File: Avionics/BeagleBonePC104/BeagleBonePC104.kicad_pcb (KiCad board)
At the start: 2 copper layers, 90.2 x 95.9 mm, 17 parts, among them U4 TJA1051T-3, U5 TMP36xS

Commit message: Ian Golberg - Tentatively Finalized v3 of the flight computer board.
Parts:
- added C2: 0.1µF, Capacitor_SMD:C_0805_2012Metric, F.Cu at (98.8, 155.4)
- added D4: CAN_PWR, LED_SMD:LED_0805_2012Metric, F.Cu at (160.9, 150.9)
- added D5: TEMP_PWR, LED_SMD:LED_0805_2012Metric, F.Cu at (160.9, 153.1)
- added D6: CLK_PWR, LED_SMD:LED_0805_2012Metric, F.Cu at (160.9, 155.3)
- added R6: 15, Resistor_SMD:R_0805_2012Metric, F.Cu at (166.0, 150.9)
- added R7: 15, Resistor_SMD:R_0805_2012Metric, F.Cu at (166.0, 153.1)
- added R8: 15, Resistor_SMD:R_0805_2012Metric, F.Cu at (166.0, 155.3)
- added TP1: TestPoint, TestPoint:TestPoint_Keystone_5000-5004_Miniature, F.Cu at (114.1, 157.2)
- added TP2: TestPoint, FlightCompuer:TestPointPad, F.Cu at (90.9, 165.8)
- added TP3: TestPoint, FlightCompuer:TestPointPad, F.Cu at (83.9, 158.6)
- added TP4: TestPoint, FlightCompuer:TestPointPad, F.Cu at (95.5, 153.9)
- added U3: ~, FlightCompuer:831054046, F.Cu at (96.2, 155.3)
- added U6: ~, FlightCompuer:SPDT Through Hole Switch, F.Cu at (143.6, 154.2)
- added U7: ~, FlightCompuer:SPDT Through Hole Switch, F.Cu at (128.3, 154.1)
- added U8: ~, FlightCompuer:SPDT Through Hole Switch, F.Cu at (133.4, 154.1)
- added U9: ~, FlightCompuer:SPDT Through Hole Switch, F.Cu at (138.4, 154.5)
- R4: value 150 -> 100; footprint Resistor_SMD:R_0603_1608Metric -> Resistor_SMD:R_0805_2012Metric
- U2: footprint PCI104Connector:PCI104ConnectorComplete -> PCI104Connector:PC104ConnectorFootprint
- moved R2 57.2 mm to (92.6, 149.4)
- moved R1 42.8 mm to (92.6, 145.1)
- moved C1 30.3 mm to (109.9, 152.6)
- moved U5 28.7 mm to (110.2, 147.1)
- moved R9 12.1 mm to (118.4, 153.3), turned to 180 degrees
- moved D3 9.02 mm to (160.9, 148.7), turned to 180 degrees
- moved U4 8.84 mm to (118.6, 147.1)
- moved R5 8.57 mm to (166.0, 148.7), turned to 0 degrees
- moved D2 7.46 mm to (160.9, 146.5), turned to 180 degrees
- moved R4 6.96 mm to (166.0, 146.5), turned to 0 degrees
- moved D1 5.59 mm to (160.9, 144.4), turned to 180 degrees
- moved R3 5.20 mm to (166.0, 144.4), turned to 0 degrees
- moved U1 0.71 mm to (170.3, 88.1)
- moved G*** 0.49 mm to (154.5, 162.6)
- moved U2 0.16 mm to (80.0, 170.0)
- renumbered R6 to R9
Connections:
- C1 pad 1: /3V3 -> Net-(D5-A)
- R1 pad 1: /5V -> Net-(R1-Pad1)
- R2 pad 1: /5V -> Net-(R1-Pad1)
- U1 pad 23: /GPIO1_17 -> /FC_TEMP
- U1 pad 5: /5V -> Net-(R1-Pad1)
- U1 pad 6: /5V -> Net-(R1-Pad1)
- U1 pad 83: unconnected-(U1-UART5_TXD-Pad83) -> /UART_TX
- U1 pad 84: unconnected-(U1-UART5_RXD-Pad84) -> /UART_RX
- U2 pad 103: unconnected-(U2-Pad103) -> /10MHz_CLK
- U2 pad 19: unconnected-(U2-UART_1_TX-Pad19) -> /UART_TX
- U2 pad 20: unconnected-(U2-UART_1_RX-Pad20) -> /UART_RX
- U2 pad 36: /GPIO2_6 -> unconnected-(U2-Pad36)
- U2 pad 53: /FC_TEMP -> unconnected-(U2-TEMP_1-Pad53)
- U2 pad 70: unconnected-(U2-Pad70) -> /GPIO2_6
- U2 pad 80: unconnected-(U2-Pad80) -> /3V3
- U2 pad 96: /GPIO1_17 -> /FC_TEMP
- U4 pad 3: /3V3 -> Net-(D4-A)
- U4 pad 5: /3V3 -> Net-(D4-A)
- U5 pad 5: /3V3 -> Net-(D5-A)
- U5 pad 8: /3V3 -> Net-(D5-A)
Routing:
- net /GPIO1_15: track 0.00 -> 0.82 mm
- added copper zone on In2.Cu, net /3V3
- added copper zone on B.Cu, net GND
- added copper zone on In1.Cu, net GND
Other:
- board size 90.2 x 95.9 mm -> 90.2 x 96 mm
- copper layers 2 -> 4
- board text added: "10MHz Clock"
- board text added: "A"
- board text added: "Beaglebone PWR"
- board text added: "CAN"
- board text added: "CAN PWR"
- board text added: "CFPPS-73"
- board text added: "CLK"
- board text added: "CLK_PWR"
- board text added: "DO NOT APPLY VOLTAGE TO ANY PC104/GPIO PIN WHEN 5V POWER IS NOT SUPPLIED TO THE BEAGLEBONE, IT WILL DAMAGE THE PROCESSOR AND VOID THE WARRANTY. NO PINS ARE TO BE DRIVEN UNTIL AFTER THE SYS_RESET LINE GOES HIGH."
- board text added: "I2C_SCL"
- board text added: "I2C_SDA"
- board text added: "PC104 3V3"
- board text added: "PC104 5V"
- board text added: "Rev. 3.0.0 - 09.5.24 - Ian Goldberg"
- board text added: "SYS_RESETn"
- board text added: "TEMP"
- board text added: "TEMP PWR"
- board text added: "TJA1051T-3"
- board text added: "TMP36xS"
- board text added: "TURN ALL SWITCHES *OFF* BEFORE POWERING BEAGLEBONE."
- board text added: "V"
- board text added: "{dblquote}Do, or do not. There is no try.{dblquote} -Yoda"
- board text removed: "Rev. 3 - 09.5.24 - Ian Goldberg"

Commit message: Ian Goldberg - Finished Rev. 3 of the Flight Computer PCB.
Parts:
- added GND: TestPoint, TestPoint:TestPoint_Keystone_5000-5004_Miniature, F.Cu at (104.9, 157.2)
- moved U7 2.22 mm to (126.1, 154.4)
- moved U8 1.94 mm to (131.5, 154.4)
- moved U9 1.60 mm to (136.8, 154.4)
- moved U6 1.43 mm to (142.1, 154.4)
- moved R9 0.73 mm to (118.6, 152.6)
- moved C1 0.30 mm to (110.2, 152.6)
- moved C2 0.10 mm to (98.8, 155.3)
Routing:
- net /5V: track 0.00 -> 148.6 mm, vias 0 -> 3
- net /10MHz_CLK: track 0.00 -> 139.2 mm, vias 0 -> 2
- net /I2C_SCL: track 0.00 -> 122.1 mm, vias 0 -> 3
- net /I2C_SDA: track 0.00 -> 121.7 mm, vias 0 -> 3
- net /SYS_RESETn: track 0.00 -> 121.5 mm, vias 0 -> 2
- net /UART_RX: track 0.00 -> 108.1 mm, vias 0 -> 3
- net /FC_TEMP: track 0.00 -> 102.9 mm, vias 0 -> 2
- net /CAN_H: track 0.00 -> 102.6 mm, vias 0 -> 2
- net /UART_TX: track 0.00 -> 102.4 mm, vias 0 -> 3
- net /CAN_L: track 0.00 -> 99.6 mm, vias 0 -> 2
- net /CAN_SLNT: track 0.00 -> 94.9 mm, vias 0 -> 3
- net Net-(D6-A): track 0.00 -> 90.4 mm, vias 0 -> 2
- net /GPIO3_20: track 0.00 -> 77.6 mm, vias 0 -> 2
- net /GPIO0_7: track 0.00 -> 71.5 mm, vias 0 -> 2
- net /GPIO1_16: track 0.00 -> 69.7 mm, vias 0 -> 2
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- added copper zone on F.Cu, net GND
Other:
- board text added: "Rev. 3.0.0 - 09.15.24 - Ian Goldberg"
- board text removed: "Rev. 3.0.0 - 09.5.24 - Ian Goldberg"

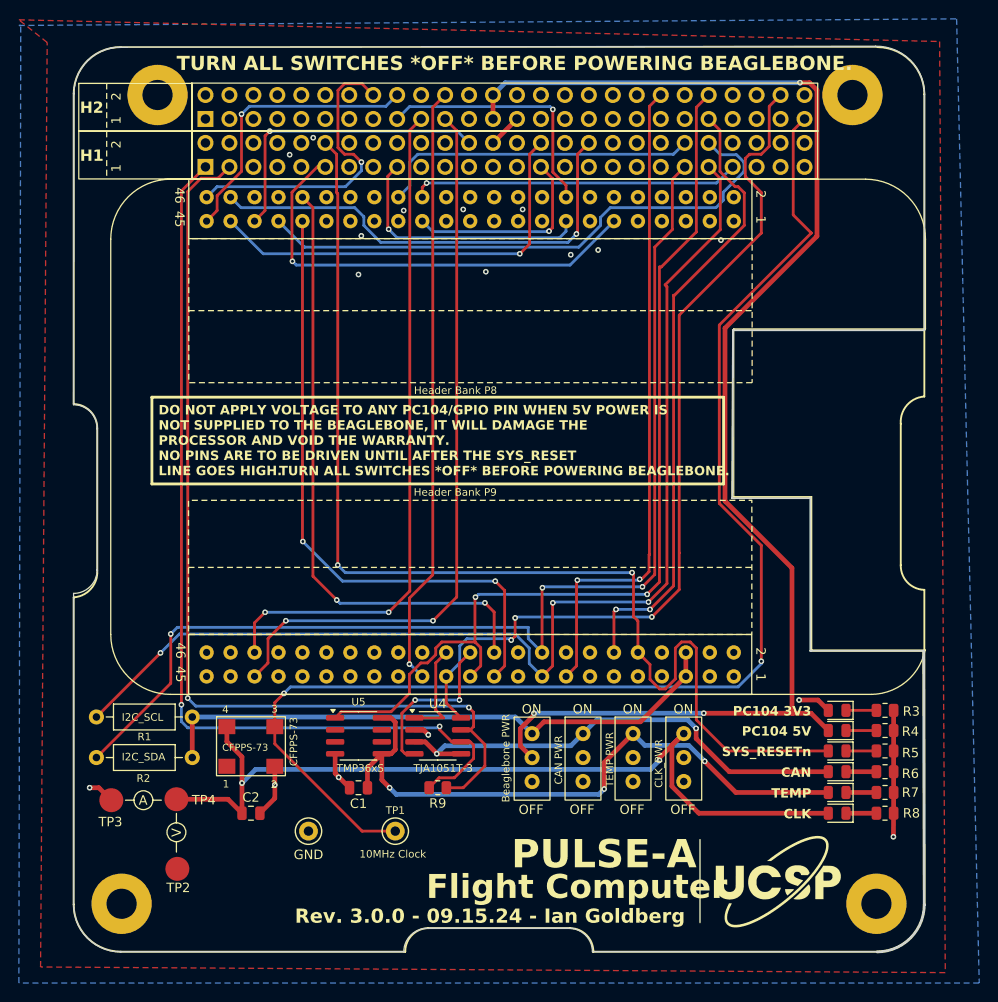
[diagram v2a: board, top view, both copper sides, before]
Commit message: Ian Goldberg - Final design for Version 3 of the Flight Computer PCB. Sending to the manufacturer now.
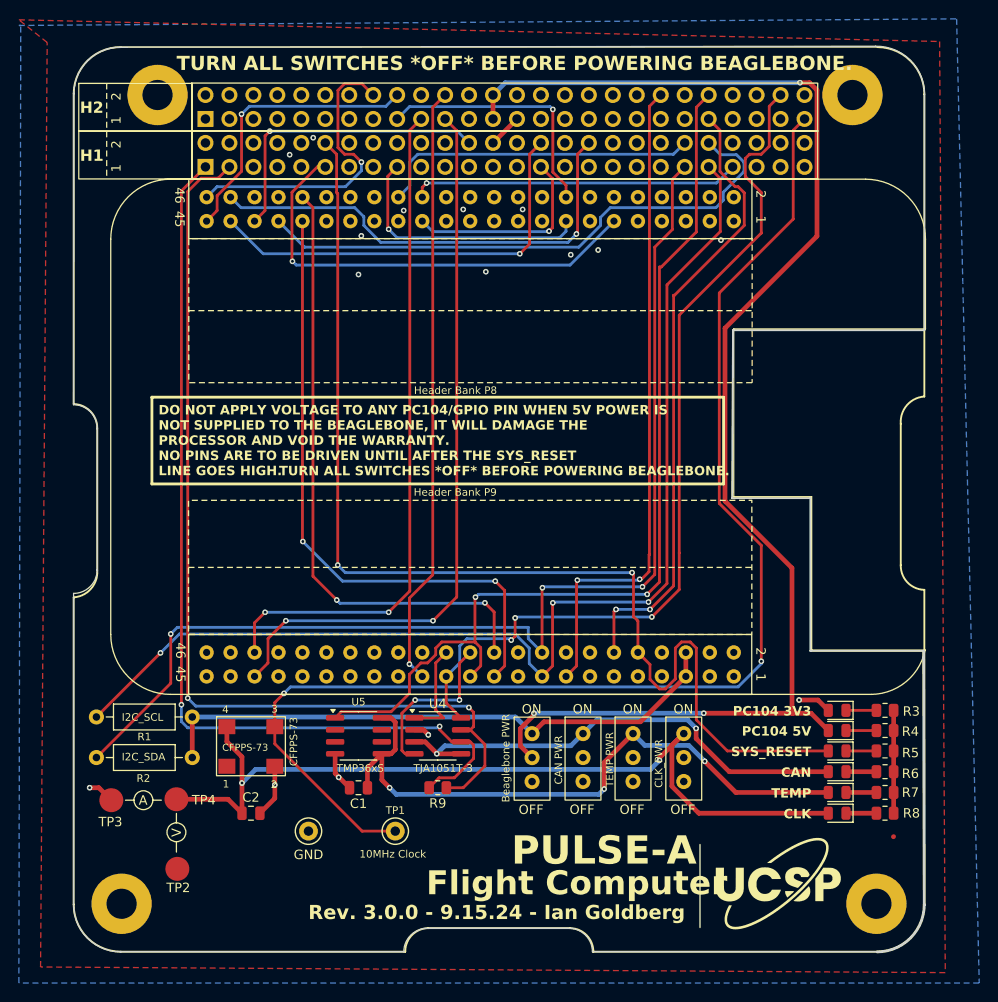
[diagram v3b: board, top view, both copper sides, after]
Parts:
- moved G*** 0.21 mm to (154.5, 162.8)
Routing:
- net GND: track 25.2 -> 22.7 mm, vias 4 -> 3
- net /10MHz_CLK: track 139.2 -> 137.6 mm
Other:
- board text added: "Rev. 3.0.0 - 9.15.24 - Ian Goldberg"
- board text added: "SYS_RESET"
- board text removed: "Rev. 3.0.0 - 09.15.24 - Ian Goldberg"
- board text removed: "SYS_RESETn"

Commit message: Ian Goldberg - Pushing preliminary versions of version 4
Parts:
- removed C2: 0.1µF, Capacitor_SMD:C_0805_2012Metric
- removed D6: CLK_PWR, LED_SMD:LED_0805_2012Metric
- removed GND, TP1: TestPoint, TestPoint:TestPoint_Keystone_5000-5004_Miniature
- removed R8: 15, Resistor_SMD:R_0805_2012Metric
- removed TP2, TP3, TP4: TestPoint, FlightCompuer:TestPointPad
- removed U6, U8, U9: ~, FlightCompuer:SPDT Through Hole Switch
- added BT1: Battery_Cell, Battery:BatteryHolder_Keystone_106_1x20mm, B.Cu at (147.0, 115.5)
- added Q1: 2N7002, Package_TO_SOT_SMD:SOT-23, F.Cu at (91.7, 146.8)
- added R12: 10k, Resistor_SMD:R_0805_2012Metric, F.Cu at (115.2, 159.2)
- added R13: 10k, Resistor_SMD:R_0805_2012Metric, F.Cu at (144.1, 154.7)
- added RTC_MFP1: TestPoint, TestPoint:TestPoint_Keystone_5000-5004_Miniature, F.Cu at (110.0, 158.9)
- added TP5: TestPoint, TestPoint:TestPoint_Keystone_5000-5004_Miniature, F.Cu at (87.9, 158.0)
- added TP6-32.768_kHz1: TestPoint, TestPoint:TestPoint_Keystone_5000-5004_Miniature, F.Cu at (87.9, 152.3)
- added U10: MCP7940N-xSN, Package_SO:SOIC-8_3.9x4.9mm_P1.27mm, F.Cu at (115.3, 147.8)
- added U12: ~, FlightCompuer:XTAL4_SiT1533_SIT, F.Cu at (115.5, 153.6)
- added U13: ~, FlightCompuer:QFN50P400X400X100-25N, F.Cu at (144.3, 147.9)
- added U14: ~, FlightCompuer:XTAL4_SiT1533_SIT, F.Cu at (135.6, 154.0)
- R1, R2: value 5.6k -> 2.2k; footprint Resistor_THT:R_Axial_DIN0207_L6.3mm_D2.5mm_P10.16mm_Horizontal -> Resistor_SMD:R_0805_2012Metric
- U3: value ~ -> W25N01GVZEIG_TR; footprint FlightCompuer:831054046 -> FlightCompuer:SON127P800X600X80-9N
- U7: value ~ -> MAX14662; footprint FlightCompuer:SPDT Through Hole Switch -> Package_DFN_QFN:QFN-28-1EP_4x4mm_P0.4mm_EP2.6x2.6mm
- moved R2 80.7 mm to (157.3, 101.2), turned to 0 degrees
- moved R1 79.9 mm to (157.3, 98.2), turned to 0 degrees
- moved U3 29.7 mm to (125.1, 148.3)
- moved R9 19.9 mm to (98.7, 153.1)
- moved U4 19.9 mm to (98.7, 147.6)
- moved U7 11.2 mm to (135.4, 148.2)
- moved C1 3.69 mm to (106.7, 153.6)
- moved U5 3.26 mm to (107.0, 147.7)
- moved G*** 1.08 mm to (154.9, 163.8)
- moved U1 0.14 mm to (170.2, 88.2)
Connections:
- C1 pad 1: Net-(D5-A) -> /TEMP_PWR
- D3 pad 2: /SYS_RESETn -> /~{SYS_RESETn}
- D4 pad 2: Net-(D4-A) -> /CAN_PWR
- D5 pad 2: Net-(D5-A) -> /TEMP_PWR
- R2 pad 1: Net-(R1-Pad1) -> /I2C_SDA
- R2 pad 2: /I2C_SDA -> Net-(R1-Pad1)
- U1 pad 11: unconnected-(U1-UART4_RXD-Pad11) -> /GPIO1_13
- U1 pad 12: /GPIO1_28 -> /GPIO1_12
- U1 pad 14: unconnected-(U1-EHRPWM1A-Pad14) -> /GPIO1_26
- U1 pad 15: /GPIO1_16 -> /GPIO1_15
- U1 pad 16: unconnected-(U1-EHRPWM1B-Pad16) -> /GPIO1_14
- U1 pad 17: /I2C_SCL -> /GPIO1_27
- U1 pad 18: /I2C_SDA -> /GPIO2_1
- U1 pad 23: /FC_TEMP -> unconnected-(U1-GPIO1_4-Pad23)
- U1 pad 27: /GPIO3_19 -> /GPI02_22
- U1 pad 28: unconnected-(U1-SPI1_CS0-Pad28) -> /GPIO2_24
- U1 pad 29: unconnected-(U1-SPI1_D0-Pad29) -> /NAND_~{WP}(I/O2)
- U1 pad 30: unconnected-(U1-SPI1_D1-Pad30) -> /NAND_~{HOLD}(I/O3)
- U1 pad 31: unconnected-(U1-SPI1_SCLK-Pad31) -> /SPI_SCLK
- U1 pad 39: unconnected-(U1-AIN0-Pad39) -> /GPIO2_12
- U1 pad 4: unconnected-(U1-DC_3.3V-Pad4) -> Net-(R1-Pad1)
- U1 pad 40: unconnected-(U1-AIN1-Pad40) -> /FC_TEMP
- U1 pad 41: /GPIO3_20 -> /GPIO2_10
- U1 pad 43: GND -> /GPIO2_8
- U1 pad 44: GND -> /GPIO2_9
- U1 pad 45: GND -> /MSP430_RST
- U1 pad 46: GND -> /10MHz_CLK_STANDBY
- U1 pad 47: GND -> (no net)
- U1 pad 48: GND -> (no net)
- U1 pad 49: unconnected-(U1-GPIO1_6-Pad49) -> (no net)
- U1 pad 5: Net-(R1-Pad1) -> /5V
- U1 pad 50: unconnected-(U1-GPIO1_7-Pad50) -> (no net)
- U1 pad 51: unconnected-(U1-GPIO1_2-Pad51) -> (no net)
- U1 pad 52: unconnected-(U1-GPIO1_3-Pad52) -> (no net)
- U1 pad 53: unconnected-(U1-TIMER4-Pad53) -> (no net)
- U1 pad 54: unconnected-(U1-TIMER7-Pad54) -> (no net)
- U1 pad 55: unconnected-(U1-TIMER5-Pad55) -> (no net)
- U1 pad 56: unconnected-(U1-TIMER6-Pad56) -> (no net)
- U1 pad 57: /GPIO1_13 -> (no net)
- U1 pad 58: /GPIO1_12 -> (no net)
- U1 pad 59: unconnected-(U1-EHRPWM2B-Pad59) -> (no net)
- U1 pad 6: Net-(R1-Pad1) -> /5V
- U1 pad 60: /GPIO1_26 -> (no net)
- U1 pad 61: /GPIO1_15 -> (no net)
- U1 pad 62: /GPIO1_14 -> (no net)
- U1 pad 63: /GPIO1_27 -> (no net)
- U1 pad 64: /GPIO2_1 -> (no net)
- U1 pad 65: unconnected-(U1-EHRPWM2A-Pad65) -> (no net)
- U1 pad 66: unconnected-(U1-GPIO1_31-Pad66) -> (no net)
- U1 pad 67: unconnected-(U1-GPIO1_30-Pad67) -> (no net)
- U1 pad 68: unconnected-(U1-GPIO1_5-Pad68) -> (no net)
- U1 pad 69: unconnected-(U1-GPIO1_4-Pad69) -> (no net)
- U1 pad 70: unconnected-(U1-GPIO1_1-Pad70) -> (no net)
- U1 pad 71: unconnected-(U1-GPIO1_0-Pad71) -> (no net)
- U1 pad 72: /GPIO1_29 -> (no net)
- U1 pad 73: /GPI02_22 -> (no net)
- U1 pad 74: /GPIO2_24 -> (no net)
- U1 pad 75: /GPIO2_23 -> (no net)
- U1 pad 76: /GPIO2_25 -> (no net)
- U1 pad 77: unconnected-(U1-UART5_CTSN-Pad77) -> (no net)
- U1 pad 78: unconnected-(U1-UART5_RTSN-Pad78) -> (no net)
- U1 pad 79: unconnected-(U1-UART4_RTSN-Pad79) -> (no net)
- U1 pad 80: unconnected-(U1-UART3_RTSN-Pad80) -> (no net)
- U1 pad 81: unconnected-(U1-UART4_CTSN-Pad81) -> (no net)
- U1 pad 82: unconnected-(U1-UART3_CTSN-Pad82) -> (no net)
- U1 pad 83: /UART_TX -> (no net)
- U1 pad 84: /UART_RX -> (no net)
- U1 pad 85: /GPIO2_12 -> (no net)
- U1 pad 86: /GPIO2_13 -> (no net)
- U1 pad 87: /GPIO2_10 -> (no net)
- U1 pad 88: /GPIO2_11 -> (no net)
- U1 pad 89: /GPIO2_8 -> (no net)
- U1 pad 90: /GPIO2_9 -> (no net)
- U1 pad 91: /GPIO2_6 -> (no net)
- U1 pad 92: /GPIO2_7 -> (no net)
- U2 pad 103: /10MHz_CLK -> unconnected-(U2-Pad103)
- U2 pad 42: /GPIO2_25 -> unconnected-(U2-Pad42)
- U2 pad 44: /GPIO2_12 -> unconnected-(U2-Pad44)
- U2 pad 46: /GPIO2_23 -> /GPIO2_12
- U2 pad 51: unconnected-(U2-Pad51) -> /SPWTDIO
- U2 pad 52: unconnected-(U2-Pad52) -> /SPWTCK
- U2 pad 68: /GPIO2_7 -> unconnected-(U2-ADCS_ENABLE-Pad68)
- U2 pad 70: /GPIO2_6 -> unconnected-(U2-ADCS_BOOT-Pad70)
- U2 pad 71: /GPIO0_7 -> unconnected-(U2-Pad71)
- U2 pad 73: /GPIO3_20 -> unconnected-(U2-Pad73)
- U2 pad 74: /GPIO3_19 -> unconnected-(U2-Pad74)
- U2 pad 92: /GPIO1_16 -> unconnected-(U2-Pad92)
- U2 pad 95: /GPIO1_28 -> unconnected-(U2-Pad95)
- U2 pad 96: /FC_TEMP -> unconnected-(U2-Pad96)
- U3 pad 1: /10MHz_CLK_STANDBY -> /SPI_CS
- U3 pad 2: GND -> /SPI_MISO
- U3 pad 3: /10MHz_CLK -> /NAND_~{WP}(I/O2)
- U3 pad 4: Net-(D6-A) -> GND
- U4 pad 3: Net-(D4-A) -> /CAN_PWR
- U4 pad 5: Net-(D4-A) -> /CAN_PWR
- U5 pad 5: Net-(D5-A) -> /TEMP_PWR
- U5 pad 8: Net-(D5-A) -> /TEMP_PWR
- U7 pad 1: Net-(R1-Pad1) -> /SWITCH_MODE_SEL
- U7 pad 2: /5V -> /3V3
- U7 pad 3: unconnected-(U7-Pad3) -> /3V3
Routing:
- net /5V: track 148.6 -> 0.00 mm, vias 3 -> 0
- net /10MHz_CLK: track 137.6 -> 0.00 mm, vias 2 -> 0
- net /I2C_SCL: track 121.9 -> 0.00 mm, vias 3 -> 0
- net /I2C_SDA: track 121.7 -> 0.00 mm, vias 3 -> 0
- net /SYS_RESETn: track 121.5 -> 0.00 mm, vias 2 -> 0
- net /UART_RX: track 108.1 -> 0.00 mm, vias 3 -> 0
- net /FC_TEMP: track 102.9 -> 0.00 mm, vias 2 -> 0
- net /CAN_H: track 102.6 -> 0.00 mm, vias 2 -> 0
- net /UART_TX: track 102.4 -> 0.00 mm, vias 3 -> 0
- net /CAN_L: track 99.6 -> 0.00 mm, vias 2 -> 0
- net /CAN_SLNT: track 94.9 -> 0.00 mm, vias 3 -> 0
- net Net-(D6-A): track 90.4 -> 0.00 mm, vias 2 -> 0
- net /GPIO3_20: track 77.6 -> 0.00 mm, vias 2 -> 0
- net /GPIO0_7: track 71.5 -> 0.00 mm, vias 2 -> 0
- net /GPIO1_16: track 69.7 -> 0.00 mm, vias 2 -> 0
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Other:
- board text added: "MAX14662"
- board text added: "MCP7940N"
- board text added: "MSP430FR2433"
- board text added: "Rev. 4.0.0 - 10.05.24 - Ian Goldberg"
- board text added: "SiT1533 32.768kHz"
- board text added: "W25N01GVZEIG TR"
- board text removed: "10MHz Clock"
- board text removed: "A"
- board text removed: "Beaglebone PWR"
- board text removed: "CAN PWR"
- board text removed: "CFPPS-73"
- board text removed: "CLK"
- board text removed: "CLK_PWR"
- board text removed: "I2C_SCL"
- board text removed: "I2C_SDA"
- board text removed: "Rev. 3.0.0 - 9.15.24 - Ian Goldberg"
- board text removed: "TEMP PWR"
- board text removed: "TURN ALL SWITCHES *OFF* BEFORE POWERING BEAGLEBONE."
- board text removed: "V"
